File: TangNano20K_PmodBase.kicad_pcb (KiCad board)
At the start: 2 copper layers, 80 x 76.7 mm, 34 parts, among them J1 Conn_01x20, J10 Conn_01x03, J11 Conn_01x03, J12 Conn_01x03, J2 Conn_01x20, J3 Conn_01x20, J4 Conn_01x20, J5 Conn_02x06_Top_Bottom, J6 Conn_02x06_Top_Bottom, J7 Conn_02x06_Top_Bottom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

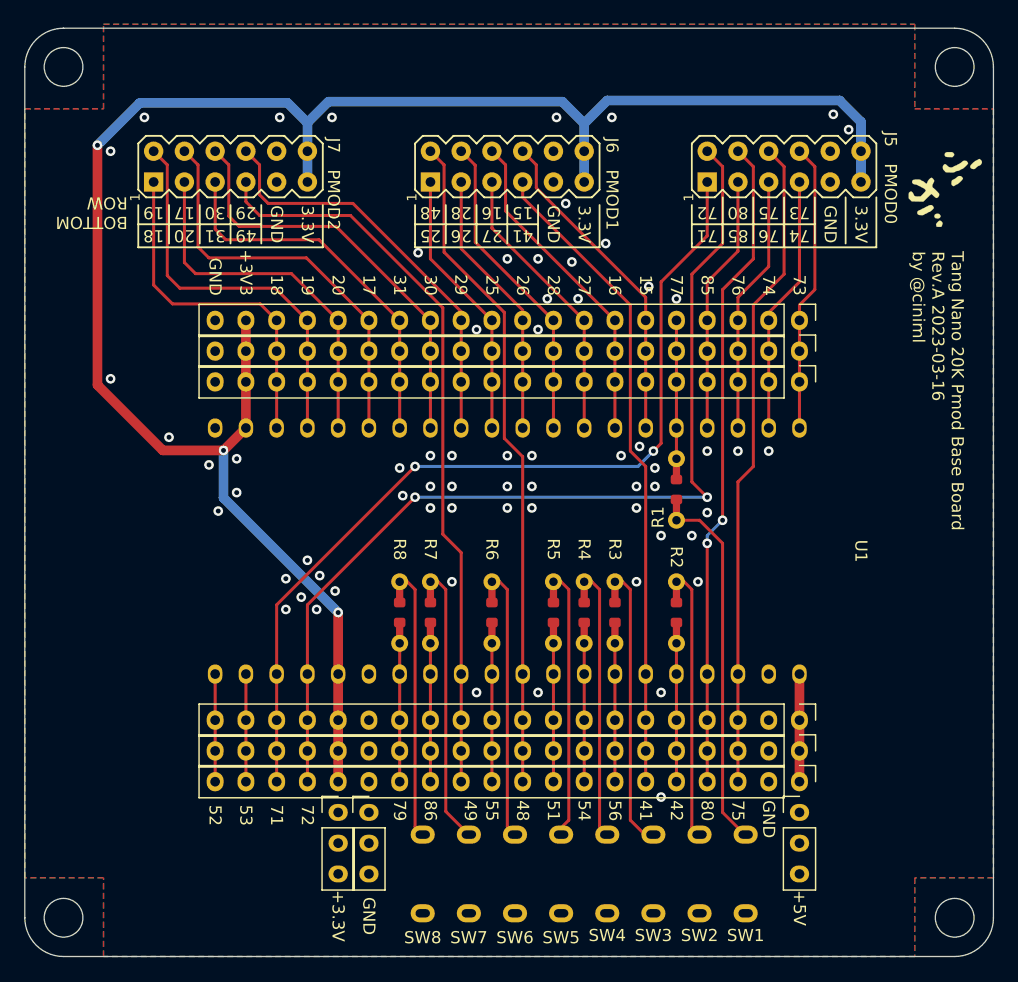
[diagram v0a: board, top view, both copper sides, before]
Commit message: Add TangNano20K PmodBase description and update to Rev.B
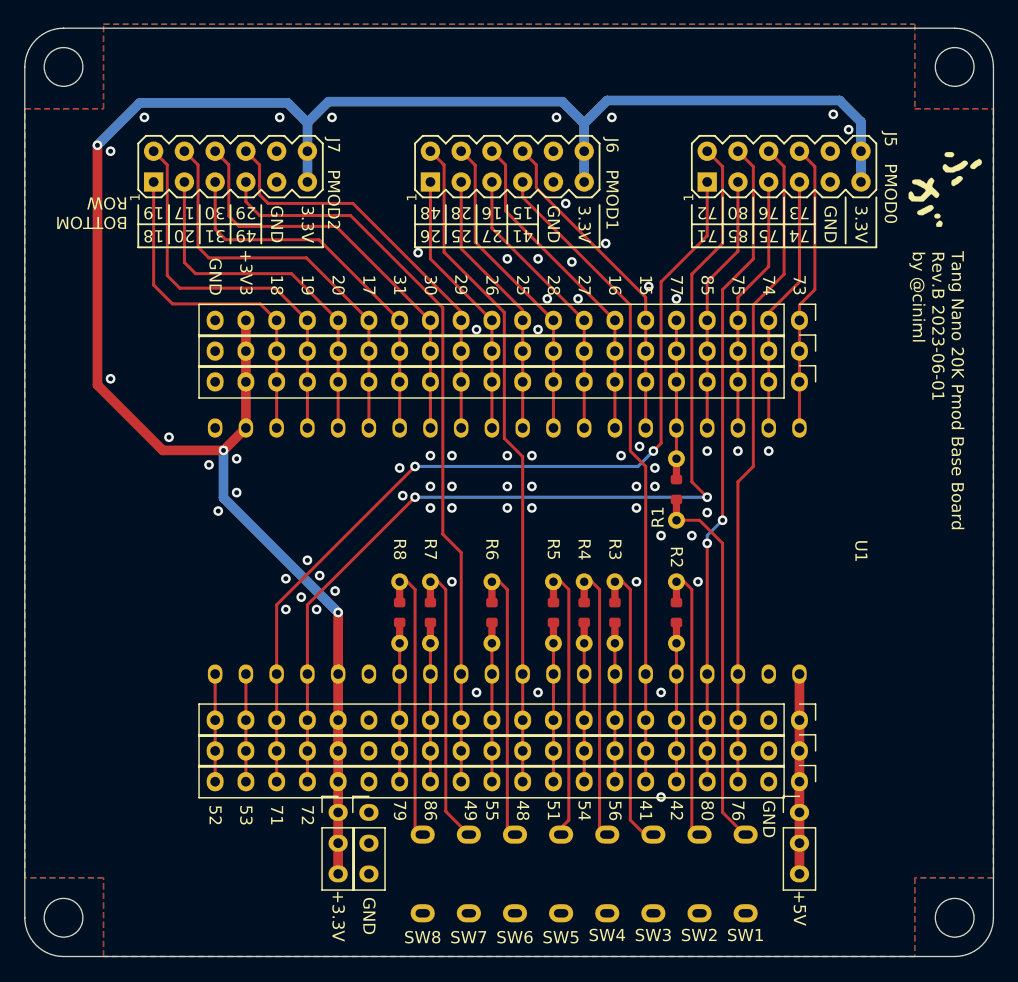
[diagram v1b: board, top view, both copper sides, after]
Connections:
- net /PMOD0_P3_PIN76 renamed /PMOD0_P3_PIN75
- net /PMOD0_P9_PIN75 renamed /PMOD0_P9_PIN76
- net /PMOD1_P1_PIN25 renamed /PMOD1_P1_PIN26
- net /PMOD1_P2_PIN26 renamed /PMOD1_P2_PIN25
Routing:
- net +5V: track 8.89 -> 16.5 mm
- net +3V3: track 158.1 -> 165.7 mm
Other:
- board text added: "Tang Nano 20K Pmod Base Board Rev.B 2023-06-01 by @ciniml"
- board text removed: "Tang Nano 20K Pmod Base Board Rev.A 2023-03-16 by @ciniml"
